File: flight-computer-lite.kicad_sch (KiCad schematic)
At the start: 24 parts, among them J1 USB_C_Receptacle_USB2.0_16P, J2 Micro_SD_Card_Det2, J3 Conn_01x02_Pin, Q1 BSS138, U1 RP2040, U2 W25Q32JVZP, U3 ICM-42688-P, U4 BMI088, U5 LIS3MDL, U6 MS5611-01BA, U7 SHT4x, U8 SAM-M8Q

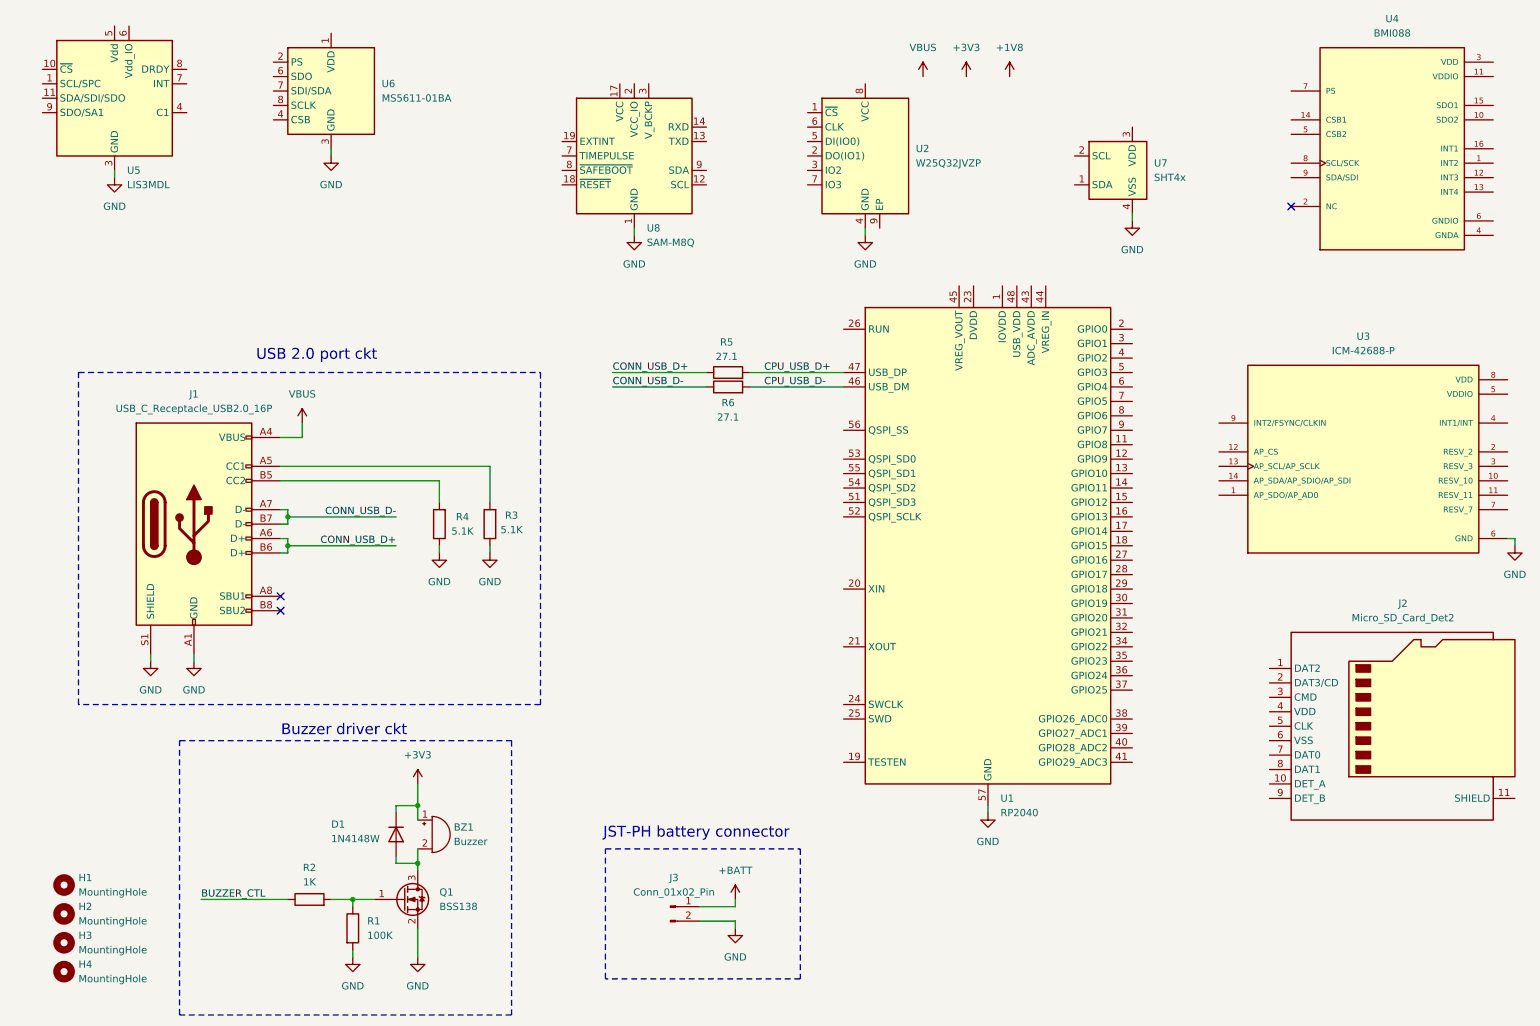
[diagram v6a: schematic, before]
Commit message: Added I2C Devices
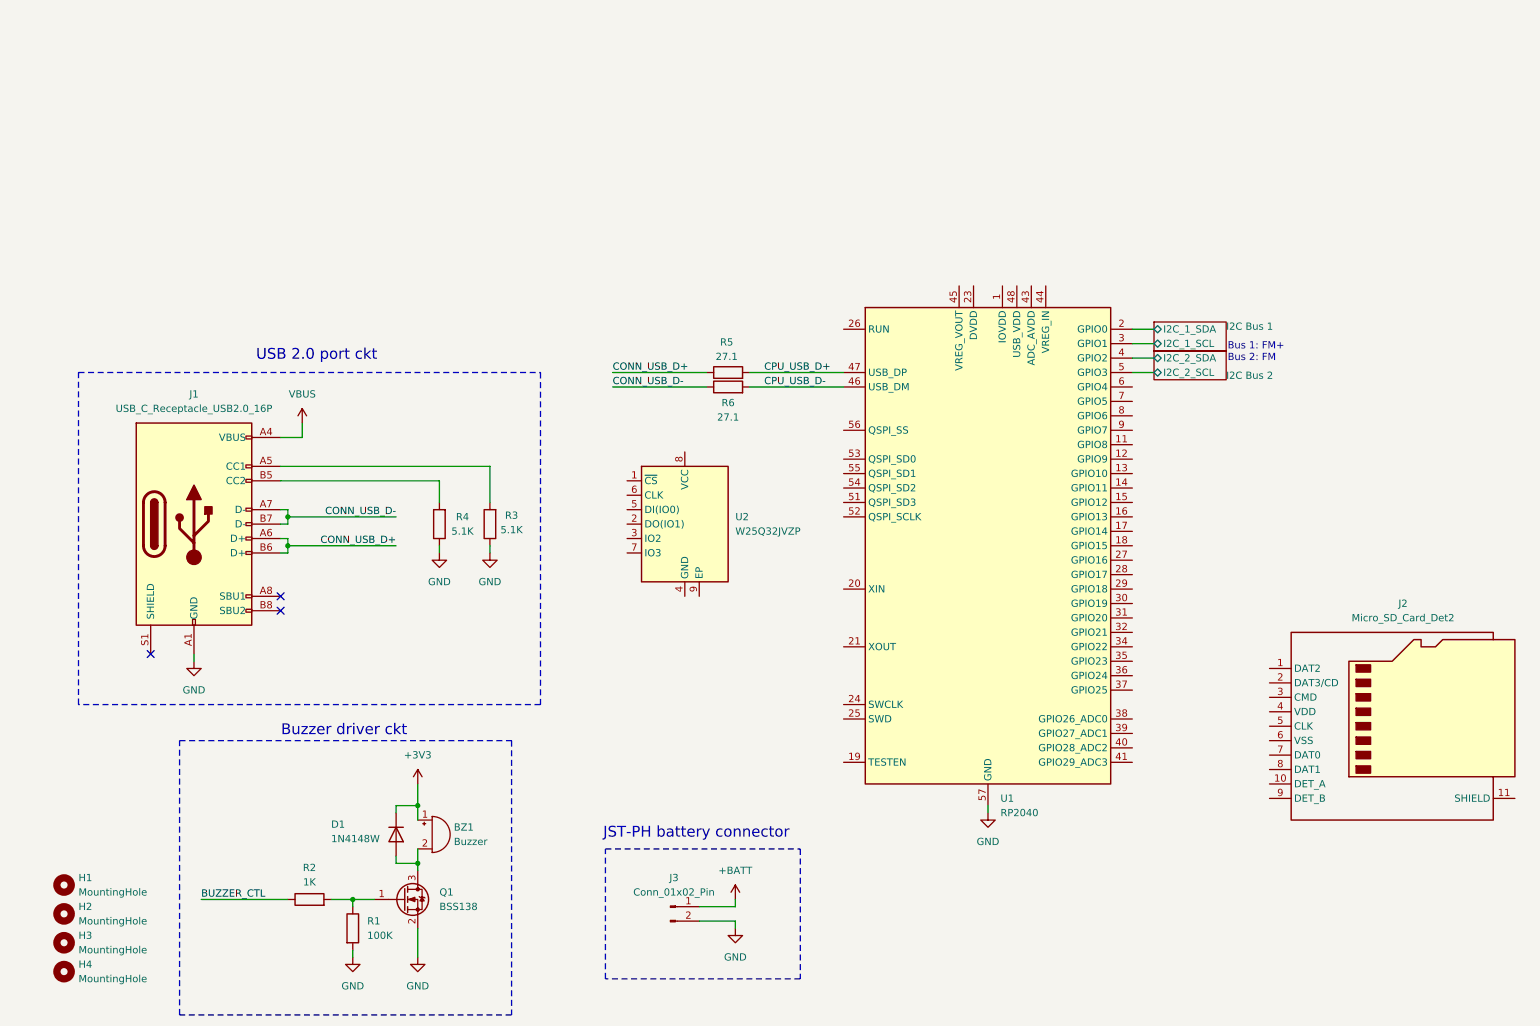
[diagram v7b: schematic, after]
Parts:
- removed U3: ICM-42688-P, LRI_partlib:PQFN50P300X250X97-14N, symbol LRI_partlib:ICM-42688-P
- removed U4: BMI088, LRI_partlib:PQFN50P450X300X100-16N, symbol LRI_partlib:BMI088
- removed U5: LIS3MDL, Package_LGA:LGA-12_2x2mm_P0.5mm, symbol Sensor_Magnetic:LIS3MDL
- removed U6: MS5611-01BA, Package_LGA:LGA-8_3x5mm_P1.25mm, symbol Sensor_Pressure:MS5611-01BA
- removed U7: SHT4x, Sensor_Humidity:Sensirion_DFN-4_1.5x1.5mm_P0.8mm_SHT4x_NoCentralPad, symbol Sensor_Humidity:SHT4x
- removed U8: SAM-M8Q, RF_GPS:ublox_SAM-M8Q, symbol RF_GPS:SAM-M8Q
- J1: footprint Connector_USB:USB_C_Receptacle_GCT_USB4105-xx-A_16P_TopMnt_Horizontal -> Connector_USB:USB_C_Receptacle_GCT_USB4110
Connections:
- net GND: no longer J1.S1 (SHIELD), U2.4 (GND)
- net I2C Bus 1/I2C_1_SDA: now reaches U1.2 (GPIO0)
- net I2C Bus 1/I2C_1_SCL: now reaches U1.3 (GPIO1)
- net I2C Bus 2/I2C_2_SDA: now reaches U1.4 (GPIO2)
- net I2C Bus 2/I2C_2_SCL: now reaches U1.5 (GPIO3)
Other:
- added sheet I2C Bus 1 (I2C_Bus_1.kicad_sch)
- added sheet I2C Bus 2 (I2C_Bus_2.kicad_sch)
- note added: "Bus 1: FM+ Bus 2: FM"
- moved on the sheet: U2

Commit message: Changed Battery Connector Footprint
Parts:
- J3: footprint Connector_JST:JST_PH_S2B-PH-K_1x02_P2.00mm_Horizontal -> Connector_JST:JST_PH_S2B-PH-SM4-TB_1x02-1MP_P2.00mm_Horizontal
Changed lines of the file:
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@@
 			)
 		)
-		(property "Footprint" "Connector_JST:JST_PH_S2B-PH-K_1x02_P2.00mm_Horizontal"
+		(property "Footprint" "Connector_JST:JST_PH_S2B-PH-SM4-TB_1x02-1MP_P2.00mm_Horizontal"
 			(at 128.27 173.99 0)
 			(effects
